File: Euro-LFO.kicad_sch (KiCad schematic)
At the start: 40 parts, among them J1 2×5 2.54 mm shrouded IDC box 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, J3 Conn_01x07_Socket, J4 Conn_01x07_Pin, J5 Conn_01x07_Socket, J6 Conn_01x07_Pin, Q1 MMBT3904, U1 TL074CDR

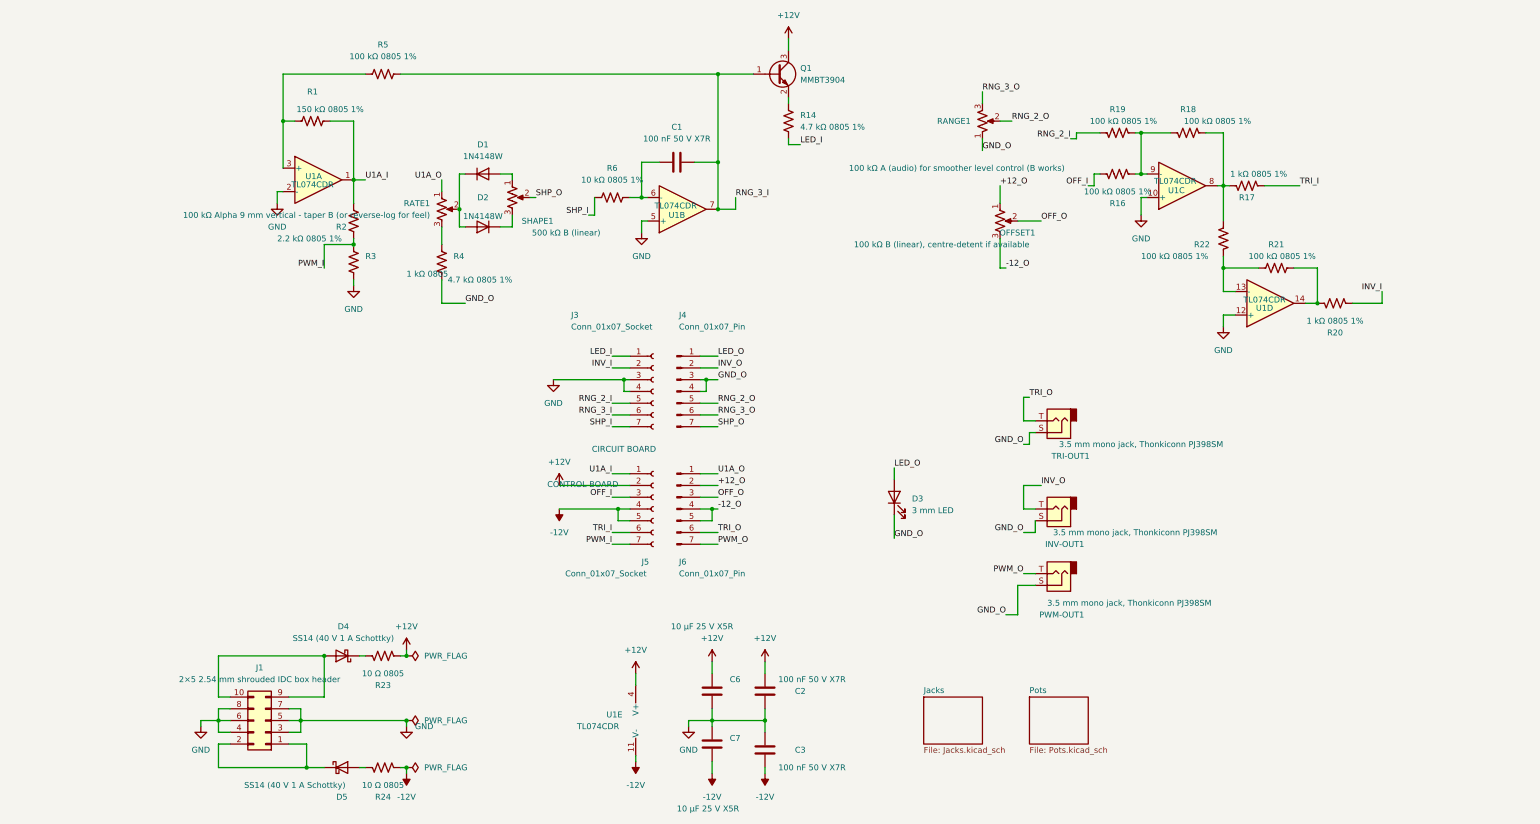
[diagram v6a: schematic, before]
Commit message: separated front panel
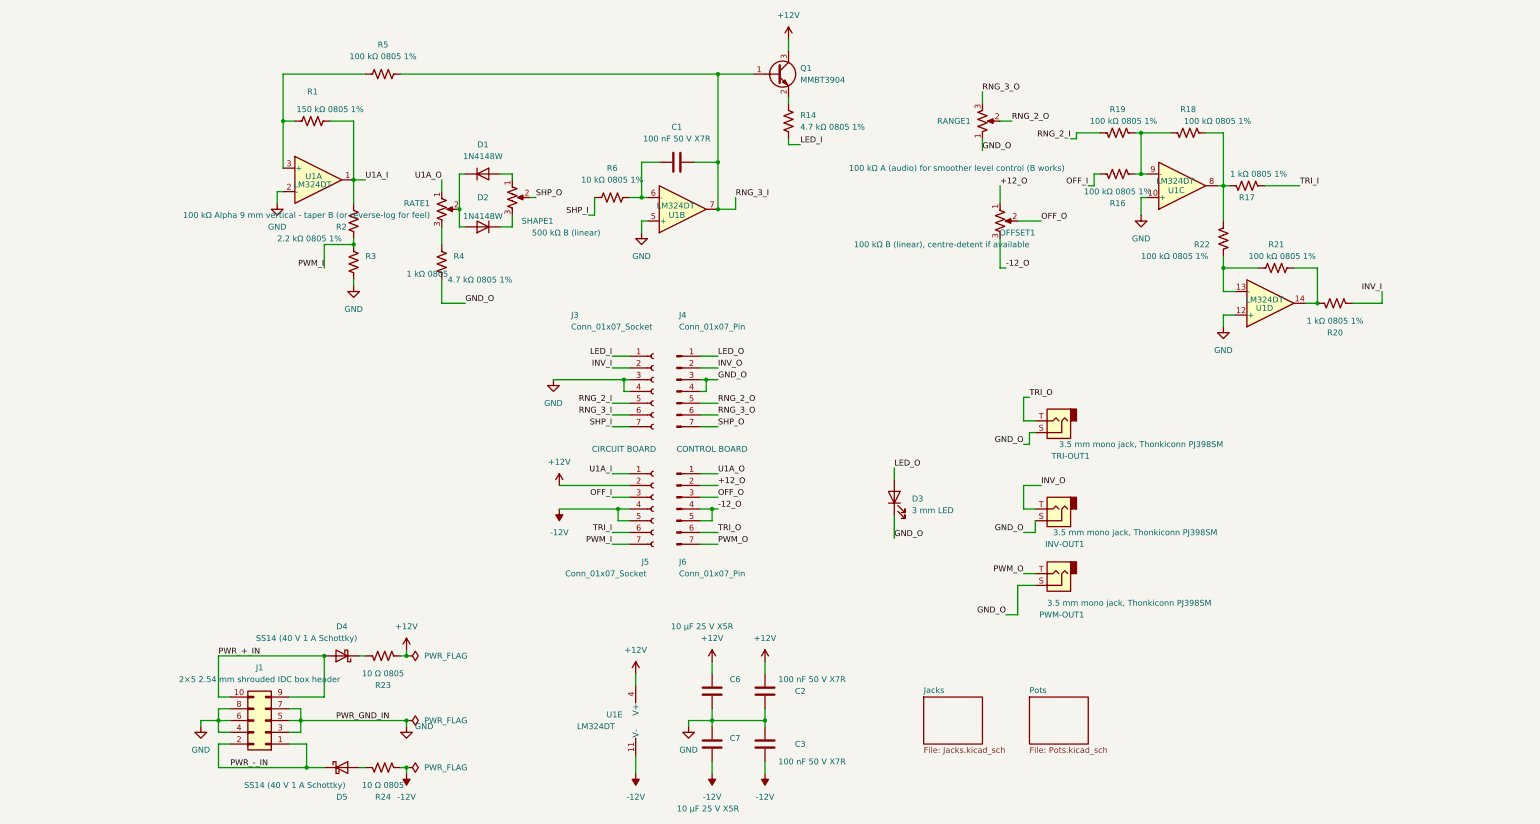
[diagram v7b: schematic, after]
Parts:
- R1: LCSC C17557 -> C17470
- R16: LCSC (none) -> C149504
- R2: LCSC C17726 -> C17520
- R23, R24: LCSC C17752 -> C17415
- U1: value TL074CDR -> LM324DT; LCSC C6961 -> C71035
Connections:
- net PWR_-_IN: now reaches D5.1 (K), J1.1 (Pin_1), J1.2 (Pin_2)
- net PWR_+_IN: now reaches D4.2 (A), J1.10 (Pin_10), J1.9 (Pin_9)
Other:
- moved on the sheet: C3
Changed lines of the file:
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@@
 	(text "CONTROL BOARD"
 		(exclude_from_sim no)
-		(at 105.41 123.19 0)
+		(at 133.35 115.57 0)
 		(effects
 			(font
@@
 	)
 	(junction
-		(at 144.78 173.99)
+		(at 78.74 63.5)
 		(diameter 0)
 		(color 0 0 0 0)
 	)
 	(junction
-		(at 78.74 63.5)
+		(at 144.78 173.99)
 		(diameter 0)
 		(color 0 0 0 0)
@@
 	(wire
 		(pts
-			(xy 144.78 173.99) (xy 144.78 176.53)
+			(xy 144.78 173.99) (xy 144.78 175.26)
 		)
 		(stroke
@@
 	(wire
 		(pts
-			(xy 116.84 181.61) (xy 116.84 182.88)
+			(xy 116.84 181.61) (xy 116.84 185.42)
 		)
 		(stroke
@@
 	(wire
 		(pts
-			(xy 144.78 184.15) (xy 144.78 185.42)
+			(xy 144.78 182.88) (xy 144.78 185.42)
 		)
 		(stroke
@@
 		)
 	)
+	(label "PWR_GND_IN"
+		(at 52.07 173.99 0)
+		(effects
+			(font
+				(size 1.27 1.27)
+			)
+			(justify left bottom)
+		)
+	)
 	(label "SHP_O"
 		(at 134.62 110.49 0)
@@
 		)
 	)
+	(label "PWR_-_IN"
+		(at 29.21 184.15 0)
+		(effects
+			(font
+				(size 1.27 1.27)
+			)
+			(justify left bottom)
+		)
+	)
 	(label "GND_O"
 		(at 172.72 134.62 0)
@@
 		)
 	)
+	(label "PWR_+_IN"
+		(at 26.67 160.02 0)
+		(effects
+			(font
+				(size 1.27 1.27)
+			)
+			(justify left bottom)
+		)
+	)
 	(label "LED_I"
 		(at 111.76 95.25 180)
@@
 			)
 		)
-		(property "Value" "TL074CDR"
+		(property "Value" "LM324DT"
 			(at 46.99 58.166 0)
 			(show_name no)
@@
 			)
 		)
-		(property "Datasheet" "http://www.ti.com/lit/ds/symlink/tl071.pdf"
+		(property "Datasheet" "https://www.st.com/resource/en/datasheet/lm324.pdf"
 			(at 49.53 52.07 0)
 			(hide yes)
@@
 			)
 		)
-		(property "Description" "Quad Low-Noise JFET-Input Operational Amplifiers, DIP-14/SOIC-14"
+		(property "Description" "Quad op-amp LM324DT (pin-compatible with TL074), SOIC-14"
 			(at 48.26 57.15 0)
 			(hide yes)
@@
 			)
 		)
-		(property "LCSC" "C6961"
+		(property "LCSC" "C71035"
 			(at 48.26 57.15 0)
 			(hide yes)
@@
 			)
 		)
-		(property "Value" "TL074CDR"
+		(property "Value" "LM324DT"
 			(at 233.426 57.404 0)
 			(show_name no)
@@
 			)
 		)
-		(property "Datasheet" "http://www.ti.com/lit/ds/symlink/tl071.pdf"
+		(property "Datasheet" "https://www.st.com/resource/en/datasheet/lm324.pdf"
 			(at 236.22 63.5 0)
 			(hide yes)
@@
 			)
 		)
-		(property "Description" "Quad Low-Noise JFET-Input Operational Amplifiers, DIP-14/SOIC-14"
+		(property "Description" "Quad op-amp LM324DT (pin-compatible with TL074), SOIC-14"
 			(at 234.95 58.42 0)
 			(hide yes)
@@
 			)
 		)
-		(property "LCSC" "C6961"
+		(property "LCSC" "C71035"
 			(at 234.95 58.42 0)
 			(hide yes)
@@
 			)
 		)
-		(property "LCSC" "C17752"
+		(property "LCSC" "C17415"
 			(at 62.23 184.15 90)
 			(hide yes)
@@
 			)
 		)
+		(property "LCSC" "C149504"
+			(at 220.98 55.88 0)
+			(hide yes)
+			(show_name no)
+			(do_not_autoplace no)
+			(effects
+				(font
+					(size 1.27 1.27)
+				)
+			)
+		)
 		(pin "1"
 		)
@@
 			)
 		)
-		(property "Value" "TL074CDR"
+		(property "Value" "LM324DT"
 			(at 125.476 62.738 0)
 			(show_name no)
@@
 			)
 		)
-		(property "Datasheet" "http://www.ti.com/lit/ds/symlink/tl071.pdf"
+		(property "Datasheet" "https://www.st.com/resource/en/datasheet/lm324.pdf"
 			(at 128.27 68.58 0)
 			(hide yes)
@@
 			)
 		)
-		(property "Description" "Quad Low-Noise JFET-Input Operational Amplifiers, DIP-14/SOIC-14"
+		(property "Description" "Quad op-amp LM324DT (pin-compatible with TL074), SOIC-14"
 			(at 127 63.5 0)
 			(hide yes)
@@
 			)
 		)
-		(property "LCSC" "C6961"
+		(property "LCSC" "C71035"
 			(at 127 63.5 0)
 			(hide yes)
@@
 			)
 		)
-		(property "LCSC" "C17726"
+		(property "LCSC" "C17520"
 			(at 55.88 66.04 0)
 			(hide yes)
@@
 			)
 		)
-		(property "Value" "TL074CDR"
+		(property "Value" "LM324DT"
 			(at 252.73 83.058 0)
 			(show_name no)
@@
 			)
 		)
-		(property "Datasheet" "http://www.ti.com/lit/ds/symlink/tl071.pdf"
+		(property "Datasheet" "https://www.st.com/resource/en/datasheet/lm324.pdf"
 			(at 255.27 88.9 0)
 			(hide yes)
@@
 			)
 		)
-		(property "Description" "Quad Low-Noise JFET-Input Operational Amplifiers, DIP-14/SOIC-14"
+		(property "Description" "Quad op-amp LM324DT (pin-compatible with TL074), SOIC-14"
 			(at 254 83.82 0)
 			(hide yes)
@@
 			)
 		)
-		(property "LCSC" "C6961"
+		(property "LCSC" "C71035"
 			(at 254 83.82 0)
 			(hide yes)
@@
 		(in_pos_files yes)
 		(dnp no)
-		(fields_autoplaced yes)
 		(property "Reference" "D4"
-			(at 53.6575 153.67 0)
+			(at 53.34 153.67 0)
 			(show_name no)
 			(do_not_autoplace no)
@@
 		)
 		(property "Value" "SS14 (40 V 1 A Schottky)"
-			(at 53.6575 156.21 0)
+			(at 45.72 156.21 0)
 			(show_name no)
 			(do_not_autoplace no)
@@
 			)
 		)
-		(property "LCSC" "C17752"
+		(property "LCSC" "C17415"
 			(at 62.23 160.02 90)
 			(hide yes)
@@
 	(symbol
 		(lib_id "power:-12V")
-		(at 116.84 182.88 180)
+		(at 116.84 185.42 180)
 		(unit 1)
 		(body_style 1)
@@
 		(fields_autoplaced yes)
 		(property "Reference" "#PWR016"
-			(at 116.84 179.07 0)
+			(at 116.84 181.61 0)
 			(hide yes)
 			(show_name no)
@@
 		)
 		(property "Value" "-12V"
-			(at 116.84 187.96 0)
+			(at 116.84 190.5 0)
 			(show_name no)
 			(do_not_autoplace no)
@@
 		)
 		(property "Footprint" ""
-			(at 116.84 182.88 0)
+			(at 116.84 185.42 0)
 			(hide yes)
 			(show_name no)
@@
 		)
 		(property "Datasheet" ""
-			(at 116.84 182.88 0)
+			(at 116.84 185.42 0)
 			(hide yes)
 			(show_name no)
@@
 		)
 		(property "Description" "Power symbol creates a global label with name \"-12V\""
-			(at 116.84 182.88 0)
+			(at 116.84 185.42 0)
 			(hide yes)
 			(show_name no)
@@
 			)
 		)
-		(property "Value" "TL074CDR"
+		(property "Value" "LM324DT"
 			(at 104.14 175.26 0)
 			(show_name no)
@@
 			)
 		)
-		(property "Datasheet" "http://www.ti.com/lit/ds/symlink/tl071.pdf"
+		(property "Datasheet" "https://www.st.com/resource/en/datasheet/lm324.pdf"
 			(at 120.65 168.91 0)
 			(hide yes)
@@
 			)
 		)
-		(property "Description" "Quad Low-Noise JFET-Input Operational Amplifiers, DIP-14/SOIC-14"
+		(property "Description" "Quad op-amp LM324DT (pin-compatible with TL074), SOIC-14"
 			(at 119.38 173.99 0)
 			(hide yes)
@@
 			)
 		)
-		(property "LCSC" "C6961"
+		(property "LCSC" "C71035"
 			(at 119.38 173.99 0)
 			(hide yes)
@@
 			)
 		)
-		(property "LCSC" "C17557"
+		(property "LCSC" "C17470"
 			(at 46.99 44.45 90)
 			(hide yes)
@@
 	(symbol
 		(lib_id "Device:C")
-		(at 144.78 180.34 0)
+		(at 144.78 179.07 0)
 		(unit 1)
 		(body_style 1)
@@
 		(dnp no)
 		(property "Reference" "C3"
-			(at 152.4 180.34 0)
+			(at 152.4 179.07 0)
 			(show_name no)
 			(do_not_autoplace no)
@@
 		)
 		(property "Value" "100 nF 50 V X7R"
-			(at 154.94 184.15 0)
+			(at 154.94 182.88 0)
 			(show_name no)
 			(do_not_autoplace no)
@@
 		)
 		(property "Footprint" "Capacitor_SMD:C_0805_2012Metric"
-			(at 145.7452 184.15 0)
+			(at 145.7452 182.88 0)
 			(hide yes)
 			(show_name no)
@@
 		)
 		(property "Datasheet" ""
-			(at 144.78 180.34 0)
+			(at 144.78 179.07 0)
 			(hide yes)
 			(show_name no)
@@
 		)
 		(property "Description" "Unpolarized capacitor"
-			(at 144.78 180.34 0)
+			(at 144.78 179.07 0)
 			(hide yes)
 			(show_name no)
@@
 		)
 		(property "LCSC" "C49678"
-			(at 144.78 180.34 0)
+			(at 144.78 179.07 0)
 			(hide yes)
 			(show_name no)
